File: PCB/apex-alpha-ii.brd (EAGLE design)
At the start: 13.1 x 74.7 mm, 31 parts, among them IC1 CC430F5135, Y1 26MHz

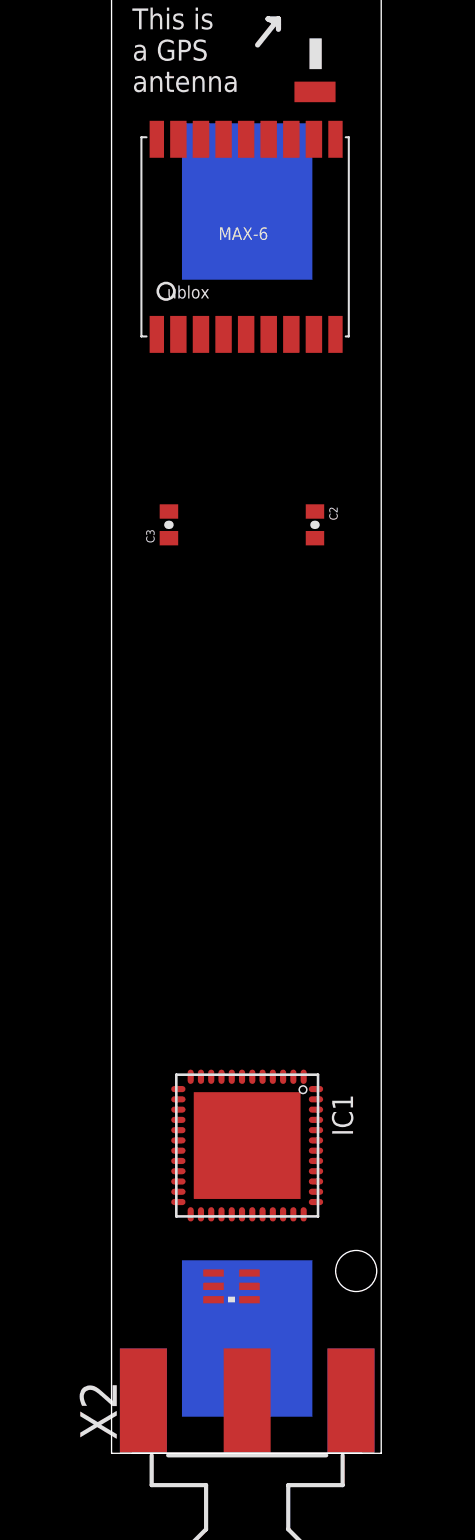
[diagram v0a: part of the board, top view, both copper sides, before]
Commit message: Replaced AAA holder with CR123A holder
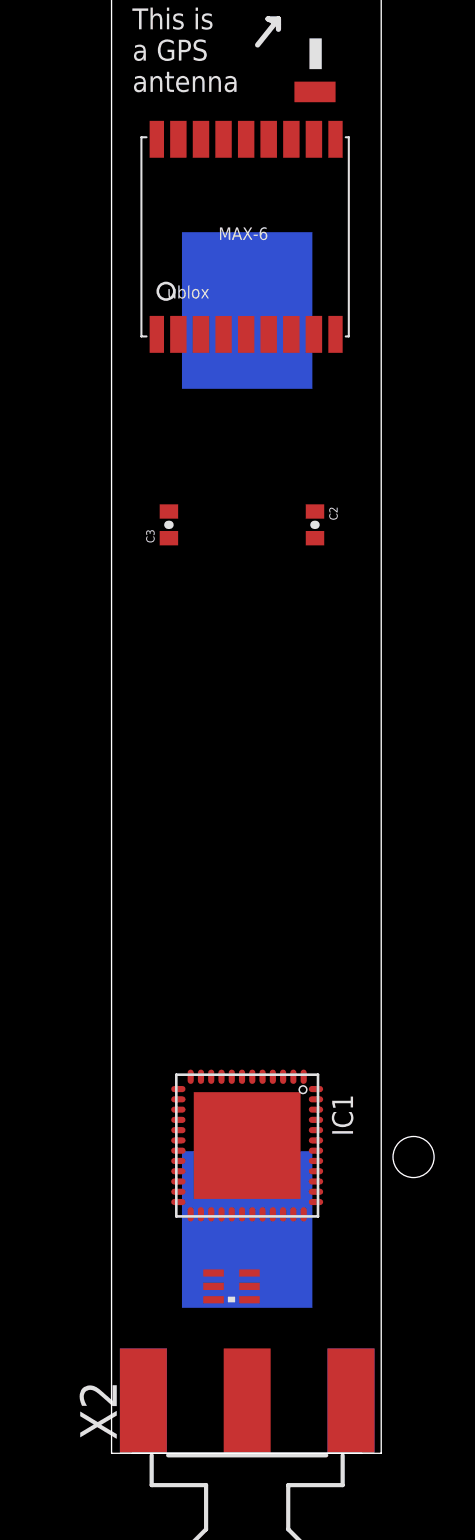
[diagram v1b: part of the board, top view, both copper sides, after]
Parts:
- removed AAA: (no value), apex:SMD-BATTERY-HOLDER-AAA
- added CR123A: (no value), apex:SMD-BATTERY-HOLDER-CR123A
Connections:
- net GND: now also CR123A.GND; no longer AAA.GND
- net N$3: now also CR123A.+V; no longer AAA.+V
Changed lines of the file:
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@@
 <element name="GPS" library="Ava" package="UBLOX_MAX-6" value="UBLOX_MAX-6" x="6.604" y="59.436" rot="R270"/>
 <element name="U$1" library="Ava" package="JTI_ANTENNA-1575AT43A40" value="JTI_ANTENNA-1575AT43A40" x="8.636" y="70.104" rot="R90"/>
-<element name="AAA" library="apex" package="SMD-BATTERY-HOLDER-AAA" value="" x="6.604" y="33.274" rot="MR90"/>
+<element name="CR123A" library="apex" package="SMD-BATTERY-HOLDER-CR123A" value="" x="6.604" y="33.274" rot="MR90"/>
 <element name="C2" library="apex" package="0402-CAP" value="1uF" x="9.906" y="45.212" rot="R270"/>
 <element name="C3" library="apex" package="0402-CAP" value="1uF" x="2.794" y="45.212" rot="R90"/>
@@
 <contactref element="X2" pad="G@3"/>
 <contactref element="X2" pad="G@4"/>
-<contactref element="AAA" pad="GND"/>
+<contactref element="CR123A" pad="GND"/>
 <contactref element="C2" pad="1"/>
 <contactref element="C3" pad="2"/>
@@
 <contactref element="VREG" pad="2"/>
 <wire x1="8.754" y1="63.986" x2="10.904" y2="63.986" width="0" layer="19" extent="1-1"/>
-<wire x1="6.604" y1="60.96" x2="8.754" y2="63.986" width="0" layer="19" extent="1-16"/>
-<wire x1="7.654" y1="54.486" x2="6.604" y2="60.96" width="0" layer="19" extent="1-16"/>
+<wire x1="6.604" y1="55.6514" x2="8.754" y2="63.986" width="0" layer="19" extent="1-16"/>
+<wire x1="7.654" y1="54.486" x2="6.604" y2="55.6514" width="0" layer="19" extent="1-16"/>
 <wire x1="2.204" y1="54.486" x2="7.654" y2="54.486" width="0" layer="19" extent="1-1"/>
 <wire x1="2.794" y1="45.862" x2="2.204" y2="54.486" width="0" layer="19" extent="1-1"/>
@@
 </signal>
 <signal name="N$3">
-<contactref element="AAA" pad="+V"/>
+<contactref element="CR123A" pad="+V"/>
 <contactref element="C2" pad="2"/>
 <contactref element="VREG" pad="1"/>
 <contactref element="VREG" pad="3"/>
 <wire x1="-56.5" y1="-13.55" x2="-57.8" y2="-13.55" width="0" layer="19" extent="1-1"/>
-<wire x1="6.604" y1="5.588" x2="-56.5" y2="-13.55" width="0" layer="19" extent="1-16"/>
-<wire x1="9.906" y1="44.562" x2="6.604" y2="5.588" width="0" layer="19" extent="1-16"/>
+<wire x1="6.604" y1="10.8966" x2="-56.5" y2="-13.55" width="0" layer="19" extent="1-16"/>
+<wire x1="9.906" y1="44.562" x2="6.604" y2="10.8966" width="0" layer="19" extent="1-16"/>
 </signal>
 </signals>
